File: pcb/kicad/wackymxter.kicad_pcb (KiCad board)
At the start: 2 copper layers, 167 x 130.1 mm, 73 parts, among them J1 OLED_128x32, J2 Conn_01x03, U1 Pico, U3 TRRS

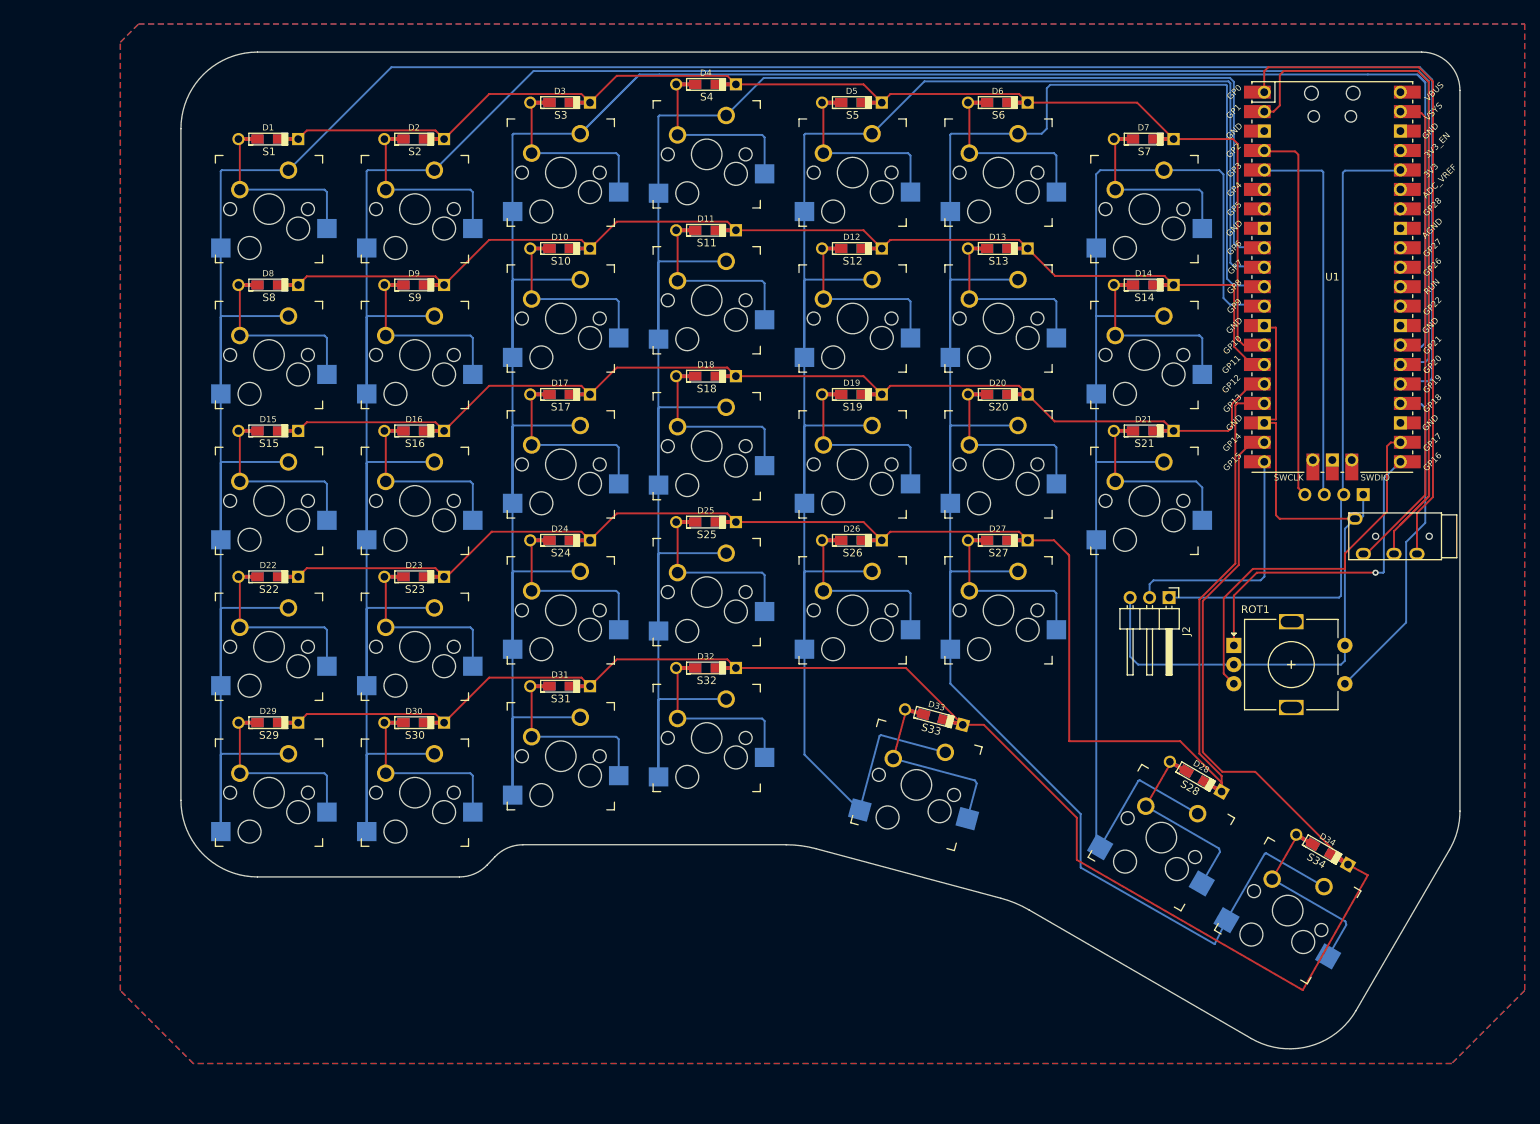
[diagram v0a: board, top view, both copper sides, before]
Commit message: [KiCAD] draft of left and right with 1.5u and fully connected
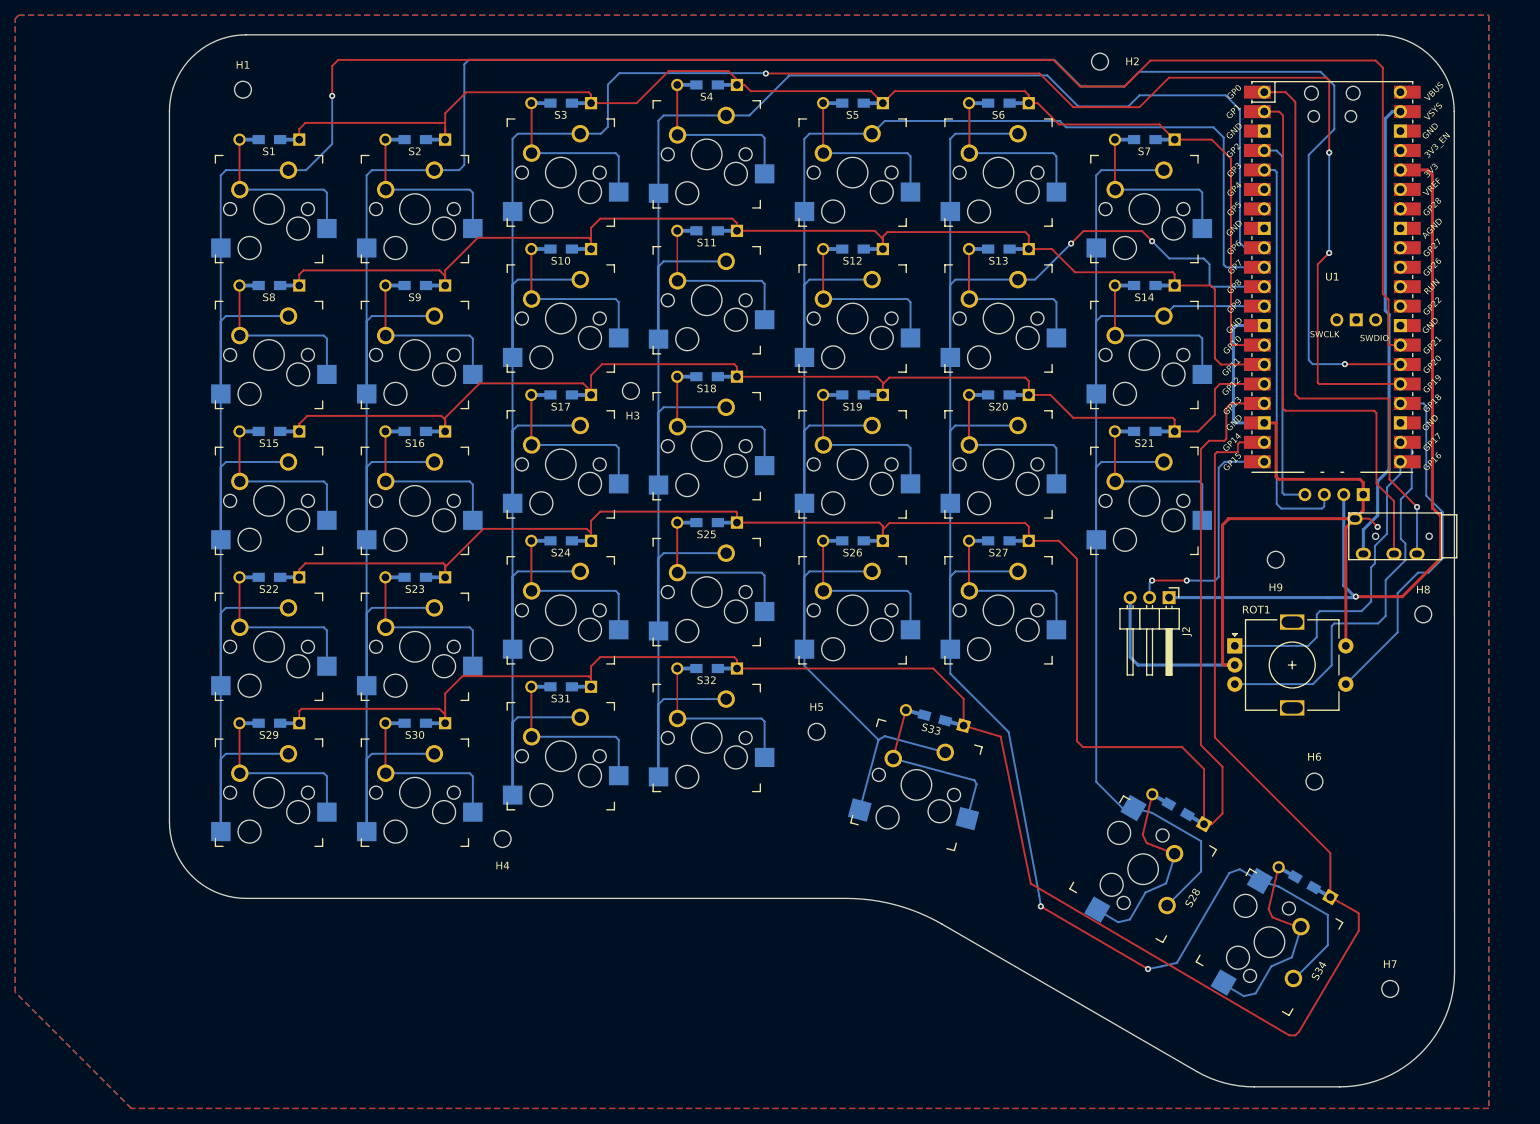
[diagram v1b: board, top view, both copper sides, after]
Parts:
- added H1: MountingHole, MountingHole:MountingHole_2.2mm_M2, F.Cu at (40.6, 26.1)
- added H2: MountingHole, MountingHole:MountingHole_2.2mm_M2, F.Cu at (152.6, 22.4)
- added H3: MountingHole, MountingHole:MountingHole_2.2mm_M2, F.Cu at (91.3, 65.4)
- added H4: MountingHole, MountingHole:MountingHole_2.2mm_M2, F.Cu at (74.5, 123.9)
- added H5: MountingHole, MountingHole:MountingHole_2.2mm_M2, F.Cu at (115.5, 109.9)
- added H6: MountingHole, MountingHole:MountingHole_2.2mm_M2, F.Cu at (180.6, 116.4)
- added H7: MountingHole, MountingHole:MountingHole_2.2mm_M2, F.Cu at (190.4, 143.5)
- added H8: MountingHole, MountingHole:MountingHole_2.2mm_M2, F.Cu at (194.8, 94.6)
- added H9: MountingHole, MountingHole:MountingHole_2.2mm_M2, F.Cu at (175.5, 87.5)
- D1, D10, D11, D12, D13, D14, D15, D16, D17, D18, D19, D2, D20, D21, D22, D23, D24, D25, D26, D27, D28, D29, D3, D30, D31, D32, D33, D34, D4, D5, D6, D7, D8, D9: footprint Keebio-Parts:Diode-dual -> Keebio-Parts:Diode-Hybrid-Back; moved to F.Cu
- U1: footprint MCU_RaspberryPi_and_Boards:RPi_Pico_SMD_TH -> RPi_Pico:RPi_PicoW_SMD_TH
- moved D28 9.06 mm to (159.4, 118.1), turned to -30 degrees
- moved D34 9.06 mm to (175.9, 127.6), turned to -30 degrees
- moved D20 7.66 mm to (135.4, 65.9), turned to 0 degrees
- moved D13 7.66 mm to (135.4, 46.9), turned to 0 degrees
- moved D27 7.66 mm to (135.4, 85.0), turned to 0 degrees
- moved D6 7.66 mm to (135.4, 27.8), turned to 0 degrees
- moved D25 7.66 mm to (97.3, 82.6), turned to 0 degrees
- moved D32 7.66 mm to (97.3, 101.7), turned to 0 degrees
- moved D11 7.66 mm to (97.3, 44.5), turned to 0 degrees
- moved D18 7.66 mm to (97.3, 63.6), turned to 0 degrees
- moved D4 7.66 mm to (97.3, 25.5), turned to 0 degrees
- moved D15 7.66 mm to (40.2, 70.7), turned to 0 degrees
- moved D16 7.66 mm to (59.2, 70.7), turned to 0 degrees
- moved D17 7.66 mm to (78.3, 65.9), turned to 0 degrees
- moved D19 7.66 mm to (116.4, 65.9), turned to 0 degrees
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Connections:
- U1 pad 25: col0 -> col2
- U1 pad 27: col2 -> col0
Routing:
- net row3: track 214.4 -> 243.0 mm
- net GND: track 99.0 -> 125.6 mm, vias 0 -> 1
- net RX0: track 98.9 -> 72.7 mm
- net row4: track 245.0 -> 269.9 mm
- net VCC: track 85.7 -> 107.3 mm, vias 0 -> 1
- net row1: track 144.8 -> 165.1 mm
- net col4: track 253.7 -> 235.4 mm
- net row2: track 140.1 -> 158.0 mm
- net row0: track 161.9 -> 175.1 mm
- net TX0: track 88.3 -> 76.9 mm, vias 0 -> 1
- net col5: track 274.6 -> 266.3 mm, vias 0 -> 4
- net col2: track 334.4 -> 327.9 mm, vias 0 -> 3
- net col1: track 346.9 -> 352.7 mm, vias 0 -> 1
- net col0: track 369.9 -> 365.2 mm, vias 0 -> 1
- net VSYS: track 64.2 -> 60.8 mm
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- added copper zone on B.Cu, net GND
- added copper zone on F.Cu, net GND
- removed copper zone on B.Cu, net (none)
- removed copper zone on F.Cu, net (none)
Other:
- board size 167 x 130.1 mm -> 167.8 x 137.4 mm
